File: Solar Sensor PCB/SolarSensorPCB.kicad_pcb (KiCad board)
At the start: 2 copper layers, 28 parts, among them J1 Arduino_Nano_Header, P10 SERIAL, P11 SOFT_SERIAL, P2 BATT, P3 DIO, P4 LOGO1, P5 LOGO2, P6 PCB, P8 AREF, P9 AIO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

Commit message: Large update of firmware and PCB
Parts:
- removed P11: SOFT_SERIAL, matts_components:SIL-4_Grove_SIL
- D2: value PIN -> DIODE
- DISP1, SW1, SW2: moved to F.Cu
- P6: footprint REInnovationFootprint:PCB_50x100mm_PP3_CutOut -> REInnovationFootprint:PCB_50x100mm_PP3_CutOut_EdgeCut
- Q1: value PT202C -> TRANS
- moved R2 24.3 mm to (118.1, 69.2)
- moved R4 24.3 mm to (118.1, 74.3)
- moved R1 24.3 mm to (118.1, 66.7)
- moved R3 24.3 mm to (118.1, 71.8)
- moved C1 23.7 mm to (111.1, 71.1)
- moved RV1 23.4 mm to (113.7, 61.0)
- moved P9 8.26 mm to (120.0, 87.0)
- moved DISP1 3.81 mm to (108.0, 53.3), turned to 0 degrees
- moved U3 3.81 mm to (102.9, 74.9)
- moved U1 2.54 mm to (124.5, 37.5)
- moved D2 1.91 mm to (109.9, 36.8)
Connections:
- J1 pad 10: /Rx_SS -> (no net)
- J1 pad 9: /Tx_SS -> (no net)
- U3 pad 1: (no net) -> +5V
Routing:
- net /Rx_SS: track 75.8 -> 0.00 mm, vias 2 -> 0
- net /Tx_SS: track 75.3 -> 0.00 mm, vias 1 -> 0
- net Net-(C1-Pad1): track 18.3 -> 42.5 mm
- net GND: track 259.2 -> 276.1 mm, vias 1 -> 0
- net Net-(R1-Pad1): track 31.0 -> 19.3 mm
- net /SDA_I2C: track 37.6 -> 49.1 mm
- net /SW_DOWN: track 47.1 -> 58.5 mm
- net /IRR: track 118.7 -> 108.4 mm, vias 1 -> 0
- net /TEMP_DATA: track 121.4 -> 112.0 mm, vias 1 -> 0
- net /CS_ADC: track 50.9 -> 41.8 mm, vias 0 -> 1
- net +5V: track 178.2 -> 185.4 mm
- net /SW_UP: track 70.5 -> 75.7 mm, vias 0 -> 1
- net /SCL_I2C: track 36.2 -> 37.8 mm
- net Net-(J1-Pad20): track 5.13 -> 3.81 mm
- net Net-(J1-Pad22): track 5.13 -> 3.81 mm
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- added copper zone on B.Cu, net GND
- added copper zone on F.Cu, net GND
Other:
- board outline added: 50 x 100 mm
- board text added: "SOLAR SENSOR"
- board text added: "Use D2 OR Q1 as sensor NOT Both!"

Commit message: Updated PCB. Not finished yet!
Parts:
- removed DISP1: OLED_I2C, REInnovationFootprint:TH_OLED1306
- removed P2: BATT, REInnovationFootprint:Batt_Connector_Strain_Relief
- removed P3: DIO, matts_components:SIL-8_lg_pad_1mm
- removed P8: AREF, matts_components:SIL-2_solder_connect
- removed P9: AIO, matts_components:SIL-3_lg_pad_1mm
- removed Q1: TRANS, REInnovationFootprint:TO92-EBC_large_pad
- removed RV1: 5k, REInnovationFootprint:TH_PRESET_Vert_Horiz
- removed SW2: DOWN, REInnovationFootprint:SW_PUSH_SMALL_lg_pad
- removed SW3: SPST, REInnovationFootprint:SW_SPDT_R_Angle_ALIEX
- added C4: 100n, REInnovationFootprint:SM_C_0805, F.Cu at (165.7, 62.6)
- added C5: 100u, REInnovationFootprint:SM_4x5.3, F.Cu at (161.3, 81.3)
- added C6: 100n, REInnovationFootprint:SM_C_0805, F.Cu at (140.7, 74.9)
- added IC1: ATTINY85-P, REInnovationFootprint:SM_SOIC_8, F.Cu at (141.0, 80.6)
- added J2: ADC, REInnovationFootprint:SIL-4_large_pad, F.Cu at (132.7, 79.4)
- added P1: I2C_OLED, REInnovationFootprint:SIL-4_large_pad, F.Cu at (101.0, 57.8)
- added R5: 10k, REInnovationFootprint:SM0805, F.Cu at (143.5, 56.2)
- added R6: 330R, REInnovationFootprint:SM0805, F.Cu at (171.4, 80.9)
- C1: value 100n -> 10n; footprint matts_components:C1_wide_lg_pad -> REInnovationFootprint:SM_C_0805
- C2: value 100u -> 100n; footprint REInnovationFootprint:C_1V7_TH -> REInnovationFootprint:SM_C_0805
- C3: footprint matts_components:C1_wide_lg_pad -> REInnovationFootprint:SM_C_0805
- D1: value 1N5819 -> LED; footprint REInnovationFootprint:TH_Diode_1 -> REInnovationFootprint:SM0805_LED
- D2: value DIODE -> PHOTO DIODE
- J1: value Arduino_Nano_Header -> ISP; footprint REInnovationFootprint:NANO_DIP_30_600 -> REInnovationFootprint:ISP_3x2
- P10: footprint matts_components:SIL-4_Grove_SIL -> REInnovationFootprint:SIL-4_Grove_SCREW
- P6: footprint REInnovationFootprint:PCB_50x100mm_PP3_CutOut_EdgeCut -> REInnovationFootprint:PCB_50x50mm_PP3_Cutout
- R1: value 220 -> 10k; footprint REInnovationFootprint:TH_Resistor_1 -> REInnovationFootprint:SM0805
- R2: value 4K7 -> 10k; footprint REInnovationFootprint:TH_Resistor_1 -> REInnovationFootprint:SM0805
- R3: value 1k -> 10k; footprint REInnovationFootprint:TH_Resistor_1 -> REInnovationFootprint:SM0805
- R4: value 10k -> 47k; footprint REInnovationFootprint:TH_Resistor_1 -> REInnovationFootprint:SM0805
- U1: value DS18B20 -> TSV911xxLx; footprint matts_components:TO92-EBC_large_pad -> REInnovationFootprint:SM_SOT-23-5
- U2: value MCP1702-50 -> LM75B; footprint matts_components:TO92_MC1703 -> REInnovationFootprint:SM_SOIC_8
- U3: value MCP3201 -> ADS1115; footprint REInnovationFootprint:DIP-8_300_ELL -> REInnovationFootprint:SM_MSOP10-0.5
- moved P4 74.4 mm to (155.3, 46.1)
- moved C3 69.4 mm to (148.9, 57.1), turned to 180 degrees
- moved U2 61.3 mm to (159.4, 62.9), turned to 270 degrees
- moved P10 61.0 mm to (153.7, 88.9), turned to 0 degrees
- moved J1 59.6 mm to (167.6, 53.3)
- moved D2 58.6 mm to (154.9, 74.3)
- moved D1 48.4 mm to (164.2, 76.8), turned to 90 degrees
- moved P6 47.9 mm to (129.5, 102.2)
- moved U3 47.6 mm to (148.6, 61.6)
- moved C2 47.3 mm to (141.3, 71.1), turned to 180 degrees
- moved SW1 43.6 mm to (174.0, 71.1)
- moved U1 38.9 mm to (148.6, 67.9), turned to 90 degrees
- moved R2 35.0 mm to (151.1, 80.9)
- moved R1 33.1 mm to (148.0, 80.9)
- moved C1 28.8 mm to (139.7, 67.6)
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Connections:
- C1 pad 1: Net-(C1-Pad1) -> /IRR1+
- C1 pad 2: GND -> Net-(C1-Pad2)
- C2 pad 1: VCC -> GND
- C2 pad 2: GND -> +5V
- C3 pad 1: VCC -> +5V
- D1 pad 1: VCC -> /SW1
- D2 pad 1: Net-(C1-Pad1) -> Net-(C1-Pad2)
- D2 pad 2: /IRR -> GND
- J1 pad 1: /Tx -> /D1
- J1 pad 2: /Rx -> +5V
- J1 pad 3: (no net) -> /D2
- J1 pad 4: GND -> /D0
- J1 pad 5: /SW_UP -> Net-(IC1-Pad1)
- J1 pad 6: /SW_DOWN -> GND
- P4 pad 1: (no net) -> Net-(P4-Pad1)
- R1 pad 1: Net-(R1-Pad1) -> +5V
- R1 pad 2: GND -> /D0
- R2 pad 2: /TEMP_DATA -> /D2
- R3 pad 1: Net-(C1-Pad1) -> +5V
- R3 pad 2: +5V -> Net-(R3-Pad2)
- R4 pad 1: /IRR -> /IRR1+
- R4 pad 2: GND -> Net-(C1-Pad2)
- SW1 pad 1: /SW_UP -> /SW1
- U1 pad 1: +5V -> /IRR1+
- U1 pad 2: /TEMP_DATA -> GND
- U1 pad 3: GND -> Net-(C1-Pad2)
- U3 pad 1: +5V -> Net-(R5-Pad2)
- U3 pad 2: /IRR -> Net-(R3-Pad2)
- U3 pad 4: GND -> /IRR1+
- U3 pad 5: /CS_ADC -> /IRR1-
- U3 pad 6: /SDA_I2C -> Net-(J2-Pad3)
- U3 pad 7: /SCL_I2C -> Net-(J2-Pad2)
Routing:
- net GND: track 276.1 -> 0.00 mm
- net +5V: track 185.4 -> 0.00 mm, vias 1 -> 0
- net /TEMP_DATA: track 112.0 -> 0.00 mm
- net /IRR: track 108.4 -> 0.00 mm
- net /SW_UP: track 75.7 -> 0.00 mm, vias 1 -> 0
- net /SW_DOWN: track 58.5 -> 0.00 mm
- net /SDA_I2C: track 49.1 -> 0.00 mm
- net Net-(C1-Pad1): track 42.5 -> 0.00 mm
- net /CS_ADC: track 41.8 -> 0.00 mm, vias 1 -> 0
- net Net-(P2-Pad2): track 38.8 -> 0.00 mm
- net /SCL_I2C: track 37.8 -> 0.00 mm
- net VCC: track 26.7 -> 0.00 mm
- net Net-(J1-Pad16): track 22.2 -> 0.00 mm
- net Net-(R1-Pad1): track 19.3 -> 0.00 mm
- net /Tx: track 17.3 -> 0.00 mm
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- removed copper zone on B.Cu, net GND
- removed copper zone on F.Cu, net GND
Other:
- board outline removed
- board text removed: "SOLAR SENSOR"
- board text removed: "Use D2 OR Q1 as sensor NOT Both!"

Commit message: Updated PCB v0.1
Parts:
- removed P4: LOGO1, CuriousElectric3:CEC_Globe_10mm_FCU
- P6: footprint REInnovationFootprint:PCB_50x50mm_PP3_Cutout -> REInnovationFootprint:PCB_40mm_Round
- SW1: footprint REInnovationFootprint:SW_PUSH_SMALL_lg_pad -> REInnovationFootprint:SMD_SW_6x3_5
- moved P5 79.9 mm to (112.9, 117.7)
- moved SW1 69.0 mm to (128.9, 123.3), turned to 270 degrees
- moved R5 68.0 mm to (99.6, 108.0), turned to 180 degrees
- moved C4 66.3 mm to (113.2, 103.0), turned to 0 degrees
- moved J1 65.6 mm to (120.7, 99.1)
- moved R3 64.4 mm to (102.1, 108.0), turned to 180 degrees
- moved U2 63.6 mm to (115.2, 108.6)
- moved C3 63.4 mm to (106.8, 104.5)
- moved U3 63.0 mm to (106.7, 108.6)
- moved R4 59.7 mm to (111.9, 119.1), turned to 180 degrees
- moved C1 59.7 mm to (109.5, 119.1)
- moved R6 58.8 mm to (124.6, 116.5), turned to 90 degrees
- moved U1 58.7 mm to (111.8, 113.7)
- moved D2 55.7 mm to (116.2, 114.3)
- moved C2 54.6 mm to (106.7, 113.3), turned to 270 degrees
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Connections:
- net /IRR1+ renamed Net-(C1-Pad1)
- P10 pad 1: /Rx -> /D3
- P10 pad 2: /Tx -> /D4
- U3 pad 5: /IRR1- -> GND
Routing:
- net GND: track 0.00 -> 243.8 mm
- net +5V: track 0.00 -> 169.3 mm, vias 0 -> 2
- net /D0: track 0.00 -> 29.8 mm, vias 0 -> 1
- net Net-(C1-Pad1): track 0.00 -> 27.9 mm, vias 0 -> 2
- net /D3: track 0.00 -> 25.0 mm, vias 0 -> 1
- net /D4: track 0.00 -> 21.4 mm, vias 0 -> 1
- net Net-(J2-Pad3): track 0.00 -> 20.9 mm, vias 0 -> 1
- net /D2: track 0.00 -> 19.2 mm, vias 0 -> 2
- net /D1: track 0.00 -> 17.3 mm, vias 0 -> 1
- net Net-(J2-Pad2): track 0.00 -> 16.5 mm, vias 0 -> 1
- net /SDA_I2C: track 0.00 -> 15.5 mm, vias 0 -> 1
- net Net-(C1-Pad2): track 0.00 -> 12.2 mm
- net /SCL_I2C: track 0.00 -> 11.7 mm, vias 0 -> 1
- net Net-(IC1-Pad1): track 0.00 -> 9.64 mm, vias 0 -> 1
- net Net-(D1-Pad2): track 0.00 -> 7.61 mm
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
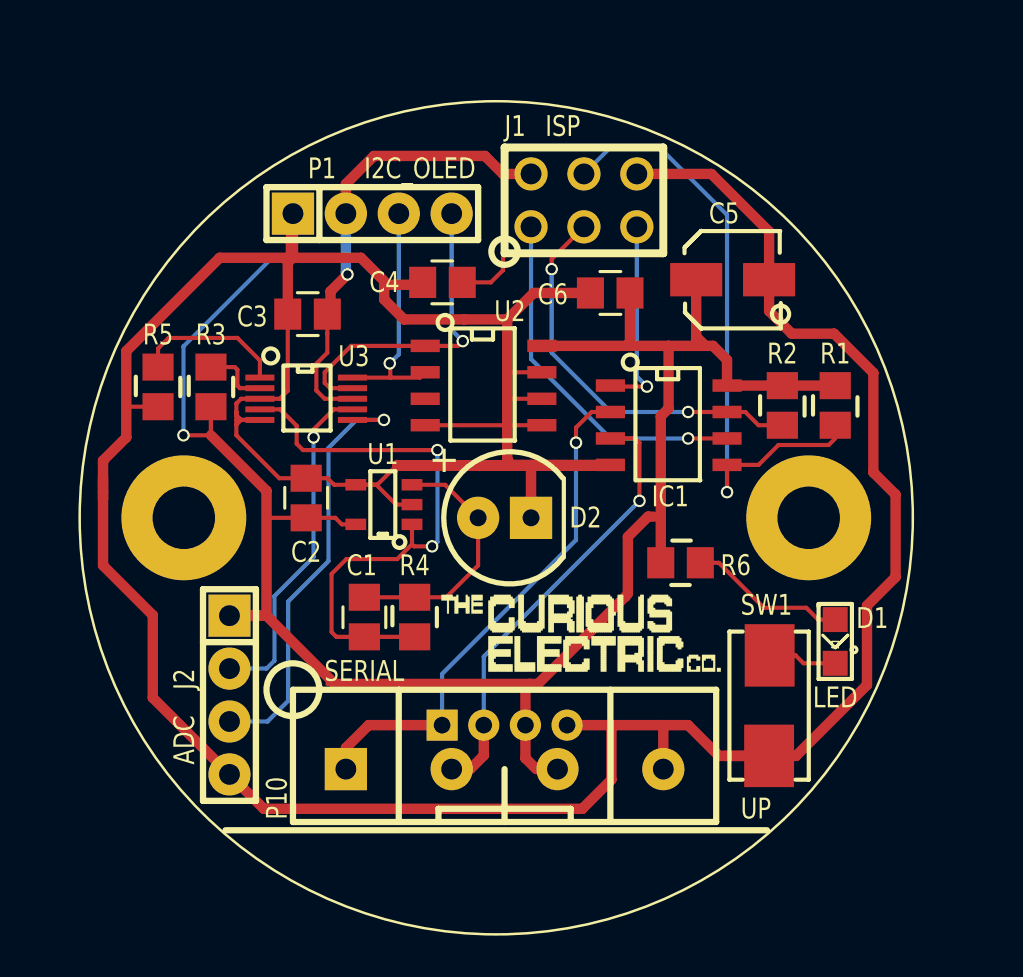
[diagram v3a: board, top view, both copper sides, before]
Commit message: Updated firmware. Updated PCB
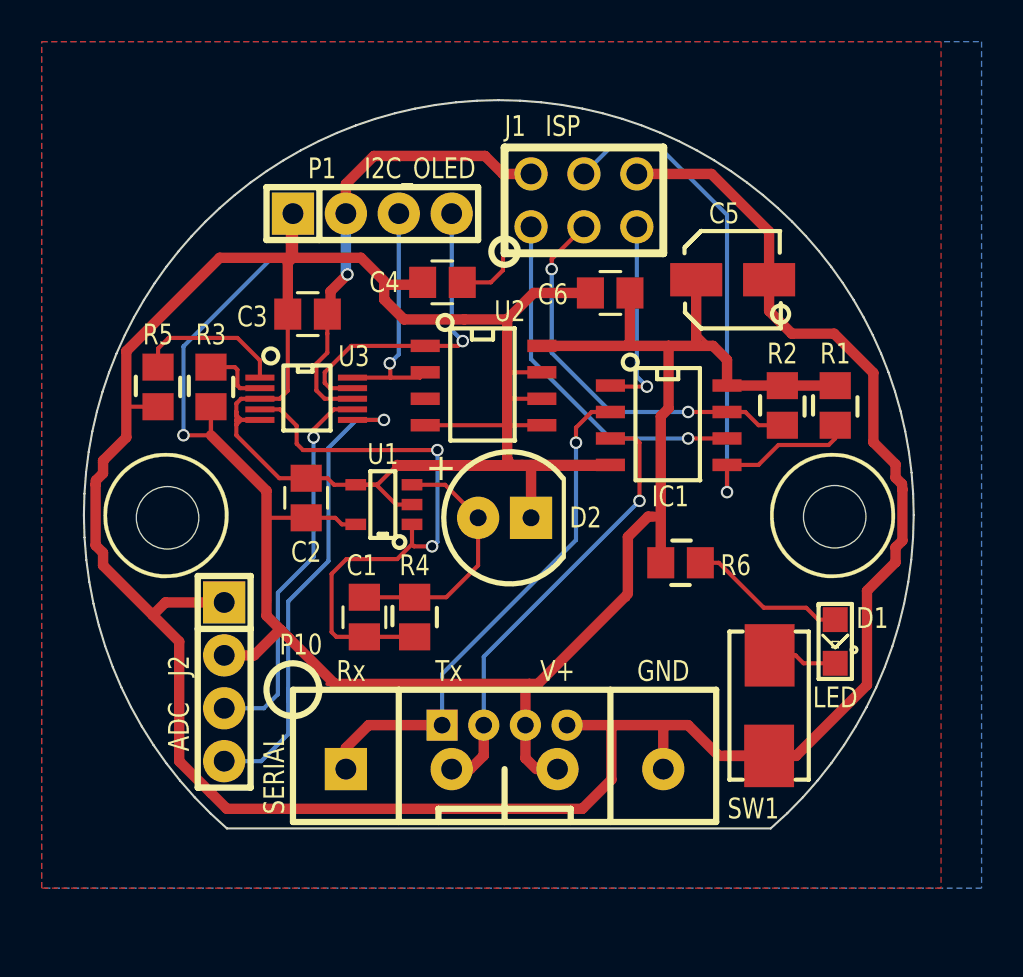
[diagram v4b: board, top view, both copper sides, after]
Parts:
- P5: moved to B.Cu
- P6: footprint REInnovationFootprint:PCB_40mm_Round -> REInnovationFootprint:PCB_40mm_Round_SolarSensorPCB_design
- moved P6 28.1 mm to (123.7, 138.0)
- moved P5 15.7 mm to (123.7, 106.3), turned to 180 degrees
- moved J2 0.68 mm to (102.7, 122.2)
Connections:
- J2 pad 1: +5V -> GND
- J2 pad 2: Net-(J2-Pad2) -> +5V
- J2 pad 4: GND -> Net-(J2-Pad4)
- U3 pad 6: Net-(J2-Pad3) -> Net-(J2-Pad4)
- U3 pad 7: Net-(J2-Pad2) -> Net-(J2-Pad3)
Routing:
- net Net-(J2-Pad4): track 0.00 -> 23.4 mm, vias 0 -> 1
- net Net-(J2-Pad2): track 16.5 -> 0.00 mm, vias 1 -> 0
- net GND: track 243.8 -> 248.0 mm
- net +5V: track 169.3 -> 165.4 mm
- net Net-(J2-Pad3): track 20.9 -> 18.5 mm
- added copper zone on B.Cu, net GND
- added copper zone on F.Cu, net GND
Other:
- board outline added: 39.8 x 35 mm
- board text added: "4/7/21 v1.0"
- board text added: "GND"
- board text added: "IRRADIANCE SENSOR"
- board text added: "Rx"
- board text added: "Tx"
- board text added: "V+"
- board text added: "www.curiouselectric.co.uk"
